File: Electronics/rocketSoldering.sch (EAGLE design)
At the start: 6 parts

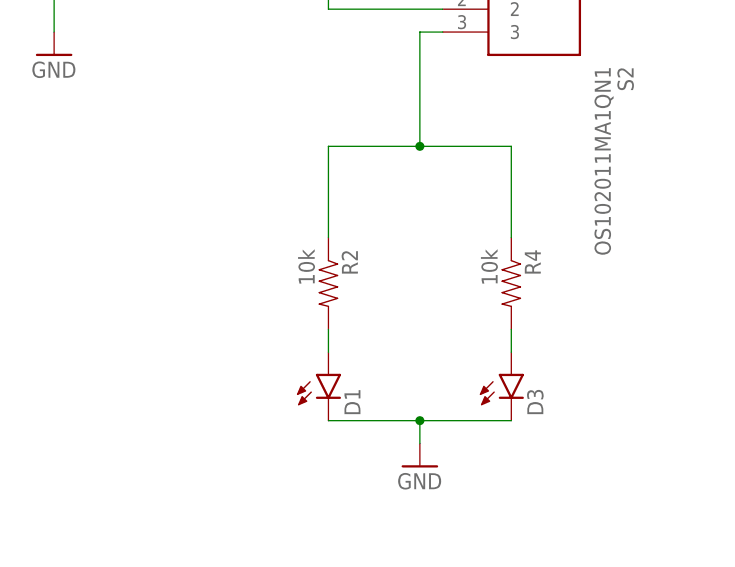
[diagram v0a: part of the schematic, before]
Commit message: Changed resistor to SMD
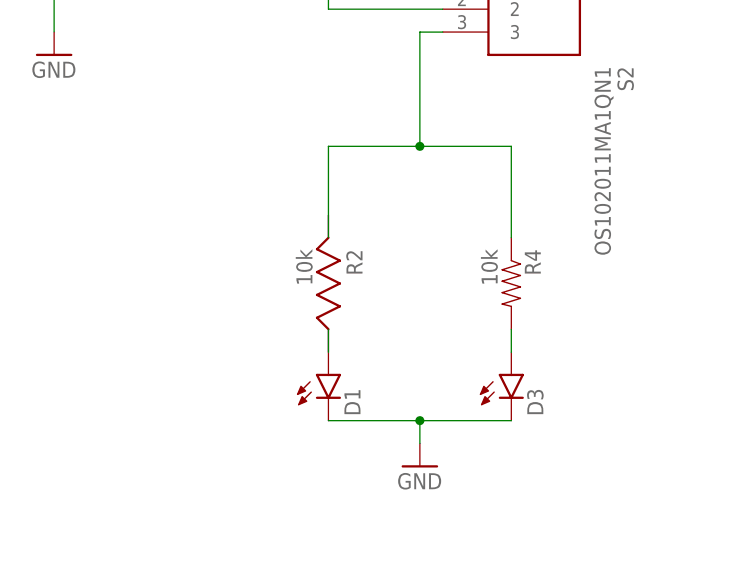
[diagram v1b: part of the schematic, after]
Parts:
- R2: device SparkFun-Passives:RESISTORAXIAL-0.3 -> Common-Parts-Library-Eagle:CRCW12060000Z0EA
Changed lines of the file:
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@@
 <part name="GND6" library="SparkFun-Aesthetics" deviceset="GND" device=""/>
 <part name="D3" library="SparkFun-LED" deviceset="LED" device="5MM"/>
-<part name="R2" library="SparkFun-Passives" deviceset="RESISTOR" device="AXIAL-0.3" value="10k"/>
+<part name="R2" library="Common-Parts-Library-Eagle" deviceset="CRCW12060000Z0EA" device="" value="10k"/>
 <part name="GND2" library="SparkFun-Aesthetics" deviceset="GND" device=""/>
 <part name="S2" library="TinkerElectric" deviceset="OS102011MA1QN1" device=""/>
@@
 <pinref part="R2" gate="G$1" pin="2"/>
 <pinref part="D1" gate="G$1" pin="A"/>
-<wire x1="142.24" y1="78.74" x2="142.24" y2="81.28" width="0.1524" layer="91"/>
+<wire x1="142.24" y1="81.28" x2="142.24" y2="78.74" width="0.1524" layer="91"/>
 </segment>
 </net>
